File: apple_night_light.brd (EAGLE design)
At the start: 100 x 55 mm, 39 parts, among them U2 INA219AIDCNR, U3 ATSHA204-TSU, Y1 16MHZ

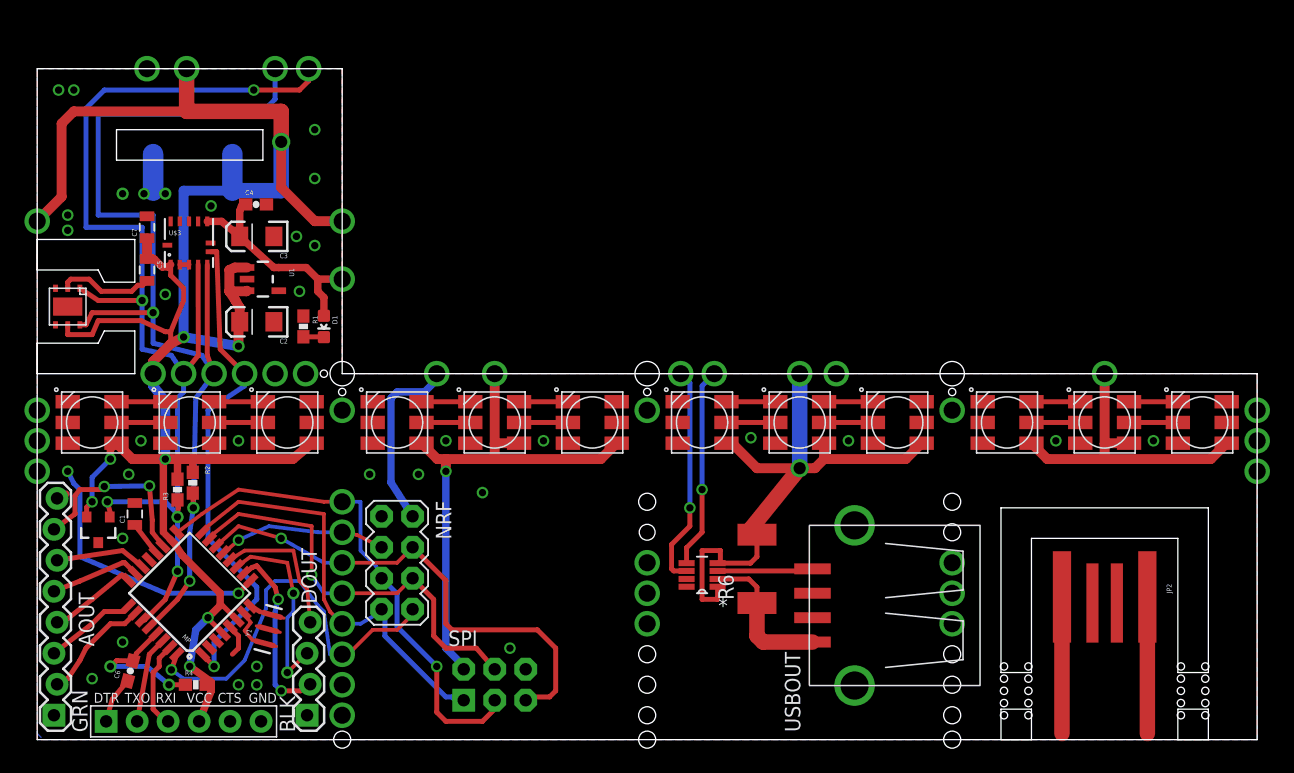
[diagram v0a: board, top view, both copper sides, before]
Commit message: re-laying out the board and separating panels to an extent
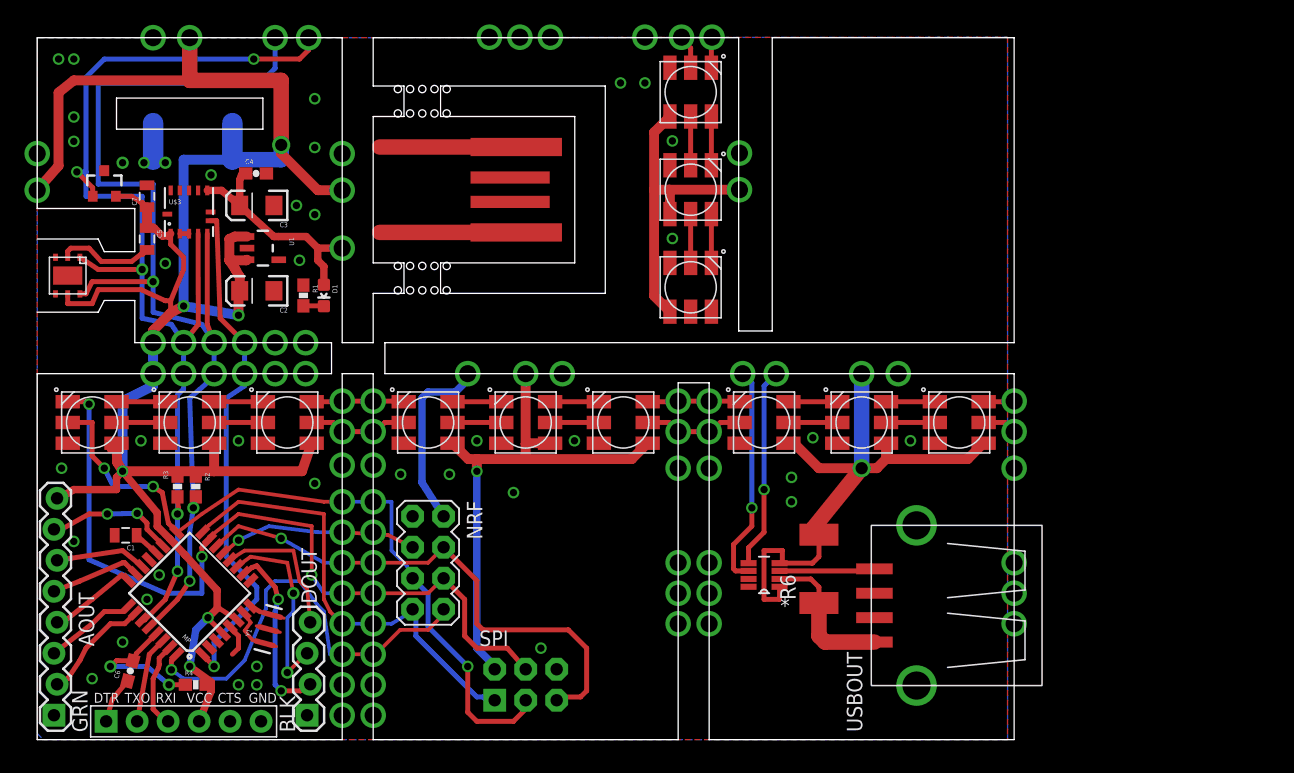
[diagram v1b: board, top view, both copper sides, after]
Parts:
- moved JP2 58.9 mm to (39.1, 45.1), turned to 180 degrees
- moved LED12 43.4 mm to (53.6, 37.1), turned to 90 degrees
- moved LED11 38.9 mm to (53.6, 45.1), turned to 90 degrees
- moved LED10 37.5 mm to (53.6, 53.1), turned to 90 degrees
- moved U3 28.3 mm to (5.50, 45.5), turned to 0 degrees
- moved LED7 5.08 mm to (59.6, 26.0)
- moved LED8 5.08 mm to (67.6, 26.0)
- moved LED9 5.08 mm to (75.6, 26.0)
- moved R6 5.08 mm to (64.1, 14.0)
- moved U2 5.08 mm to (59.6, 13.5)
- moved USBOUT 5.08 mm to (72.1, 11.0)
- moved C2 2.54 mm to (18.0, 36.8)
- moved C3 2.54 mm to (18.0, 43.8)
- moved C4 2.54 mm to (17.9, 46.4)
- moved C5 2.54 mm to (9.00, 41.0)
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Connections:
- removed net APACI: LED1.5
- removed net APADI: LED1.4
- net MOSI: now also LED1.4
- net SCK: now also LED1.5
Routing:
- net MOSI: track 34.5 -> 66.4 mm, vias 2 -> 4
- net NPIN: track 22.4 -> 0.00 mm, vias 2 -> 0
- net SCK: track 42.2 -> 60.3 mm, vias 2 -> 4
- net APACI2: track 0.00 -> 8.16 mm
- net APACI1: track 0.00 -> 8.16 mm
- net N$8: track 0.00 -> 7.58 mm
- net N$6: track 0.00 -> 7.58 mm
- net +5V: track 304.3 -> 311.1 mm, vias 17 -> 15
- net APACI3: track 0.00 -> 5.57 mm
- net N$12: track 0.00 -> 5.02 mm
- net A6: track 15.3 -> 10.7 mm
- net SCL: track 102.6 -> 105.3 mm
- net IRQ: track 32.6 -> 35.3 mm
- net MISO: track 35.0 -> 37.6 mm
- net CSN: track 41.4 -> 43.9 mm
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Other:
- board size 100 x 55 mm -> 80.1 x 57.5 mm

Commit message: adding balance board for space usage, tightening things up
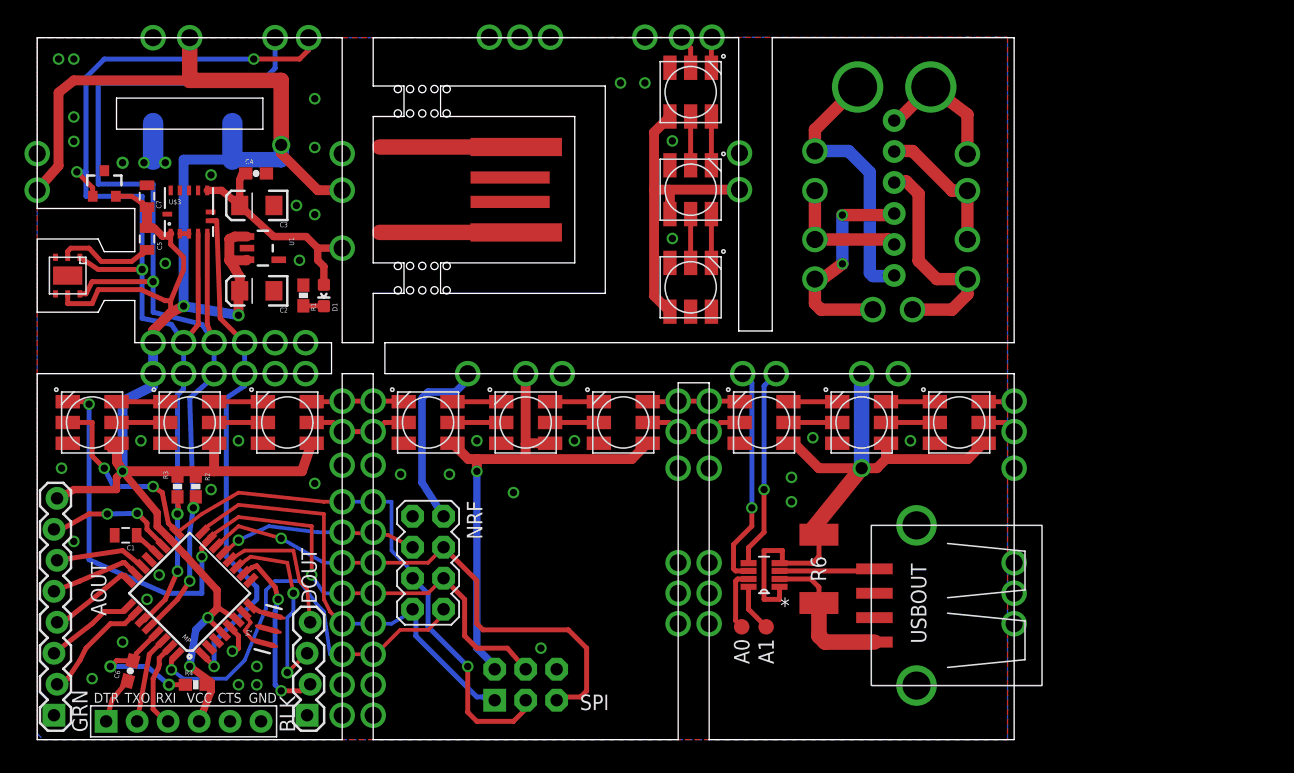
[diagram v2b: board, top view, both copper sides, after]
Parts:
- added A0, A1: TPB1,27, testpad:B1,27
- added JP3: (no value), SparkFun-Connectors:1X06_NO_SILK
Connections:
- new net N$43: A0.TP, U2.7
- new net N$44: A1.TP, U2.8
- new net N$46: AOUT.1, C1.2, C2.C, C3.C, C4.2, C5.2, C7.2, DOUT.1, JP1.P$5, JP1.P$6, JP2.GND, LED1.6, LED10.6, LED11.6, LED12.6, LED2.6, LED3.6, LED4.6, LED5.6, LED6.6, LED7.6, LED8.6, LED9.6, MP.21, MP.3, MP.5, NRF.1, R1.1, SPI.6, U$1.P$2, U$3.12, U$3.13, U$3.2, U$3.3, U1.2, U2.3, USBOUT.GND, Y1.2
- net GND: now also JP3.1; no longer AOUT.1, C1.2, C2.C, C3.C, C4.2, C5.2, C7.2, DOUT.1, JP1.P$5, JP1.P$6, JP2.GND, LED1.6, LED10.6, LED11.6, LED12.6, LED2.6, LED3.6, LED4.6, LED5.6, LED6.6, LED7.6, LED8.6, LED9.6, MP.21, MP.3, MP.5, NRF.1, R1.1, SPI.6, U$1.P$2, U$3.12, U$3.13, U$3.2, U$3.3, U1.2, U2.3, USBOUT.GND, Y1.2
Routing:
- net N$46: track 0.00 -> 40.6 mm, vias 0 -> 76
- net GND: track 33.6 -> 4.14 mm, vias 72 -> 0
- net N$55: track 0.00 -> 22.3 mm, vias 0 -> 2
- net N$49: track 0.00 -> 18.8 mm, vias 0 -> 2
- net N$51: track 0.00 -> 17.8 mm, vias 0 -> 3
- net N$47: track 0.00 -> 7.35 mm, vias 0 -> 1
- net N$45: track 0.00 -> 6.96 mm
- net N$43: track 0.00 -> 5.09 mm
- net N$48: track 0.00 -> 4.25 mm, vias 0 -> 1
- net N$53: track 0.00 -> 4.00 mm, vias 0 -> 2
- net N$44: track 0.00 -> 3.88 mm
- added copper zone on layer 1, net N$46
- added copper zone on layer 16, net N$46
- removed copper zone on layer 1, net GND
- removed copper zone on layer 16, net GND
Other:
- board text added: "+"
- board text added: "-"
- board text added: "5s balance board"
- board text added: "CUT OUT"

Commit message: final changes before order, reversing tx/rx for ftdi, reset pin on SPI
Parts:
- moved C6 0.10 mm to (7.53, 5.63), turned to 61.1 degrees
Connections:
- removed net N$22: C6.2, MP.29, R4.1
- removed net N$46: AOUT.1, C1.2, C2.C, C3.C, C4.2, C5.2, C7.2, DOUT.1, JP1.P$5, JP1.P$6, JP2.GND, LED1.6, LED10.6, LED11.6, LED12.6, LED2.6, LED3.6, LED4.6, LED5.6, LED6.6, LED7.6, LED8.6, LED9.6, MP.21, MP.3, MP.5, NRF.1, R1.1, SPI.6, U$1.P$2, U$3.12, U$3.13, U$3.2, U$3.3, U1.2, U2.3, USBOUT.GND, Y1.2
- new net RESET: C6.2, MP.29, R4.1, SPI.5
- net CSN: no longer SPI.5
- net GND: now also AOUT.1, C1.2, C2.C, C3.C, C4.2, C5.2, C7.2, DOUT.1, JP1.P$5, JP1.P$6, JP2.GND, LED1.6, LED10.6, LED11.6, LED12.6, LED2.6, LED3.6, LED4.6, LED5.6, LED6.6, LED7.6, LED8.6, LED9.6, MP.21, MP.3, MP.5, NRF.1, R1.1, SPI.6, U$1.P$2, U$3.12, U$3.13, U$3.2, U$3.3, U1.2, U2.3, USBOUT.GND, Y1.2
- net RXI: now also JP1.P$3; no longer JP1.P$2
- net TXO: now also JP1.P$2; no longer JP1.P$3
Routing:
- net RESET: track 0.00 -> 47.9 mm, vias 0 -> 4
- net N$46: track 40.6 -> 0.00 mm, vias 76 -> 0
- net GND: track 4.14 -> 44.7 mm, vias 0 -> 75
- net CSN: track 43.9 -> 20.4 mm
- net N$22: track 11.7 -> 0.00 mm, vias 2 -> 0
- net RXI: track 7.17 -> 8.15 mm, vias 0 -> 1
- added copper zone on layer 1, net GND
- added copper zone on layer 16, net GND
- removed copper zone on layer 1, net N$46
- removed copper zone on layer 16, net N$46
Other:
- outline, holes or cut-outs redrawn
- board text added: "5V"
- board text added: "A0"
- board text added: "A1"
- board text added: "A2"
- board text added: "A3"
- board text added: "A6"
- board text added: "A7"
- board text added: "D6"
- board text added: "D7"
- board text added: "D8"

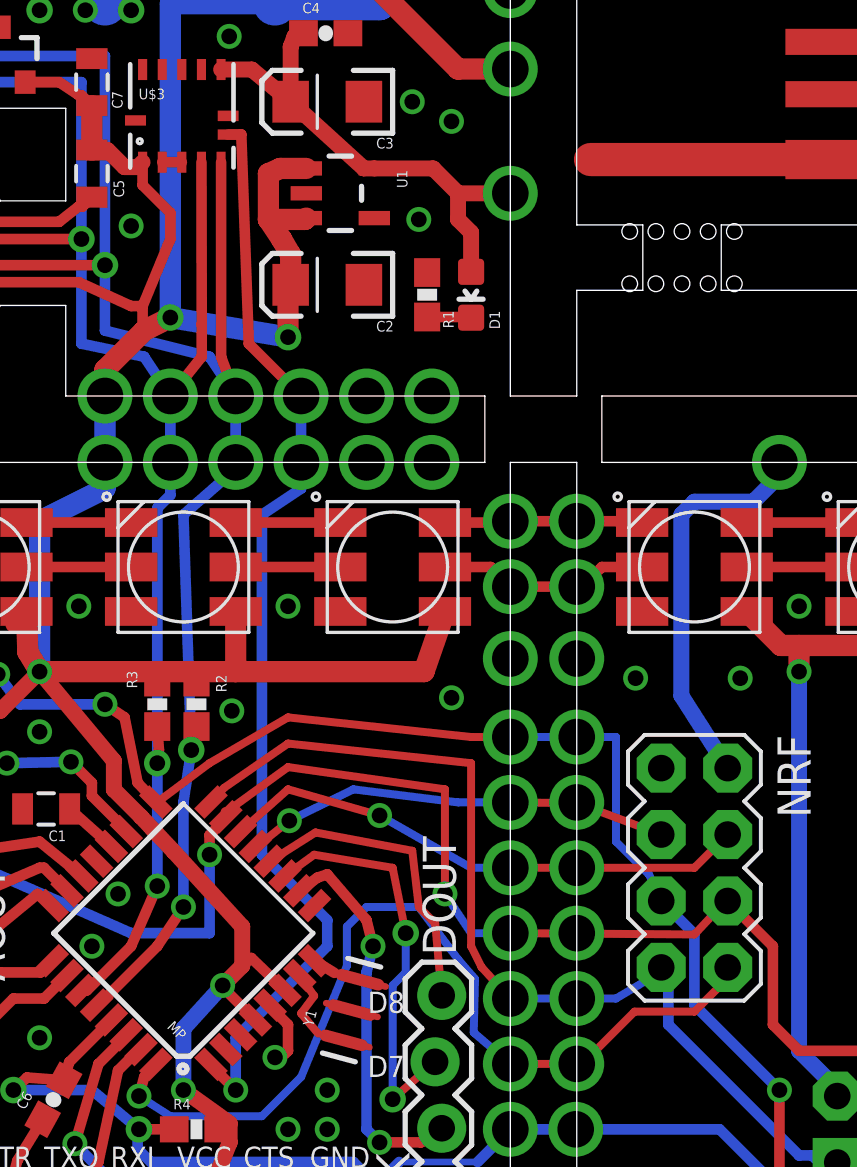
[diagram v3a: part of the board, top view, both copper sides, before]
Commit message: fixing issue with grounding VCNL IR emmiter, causes blow out of emmiter :x
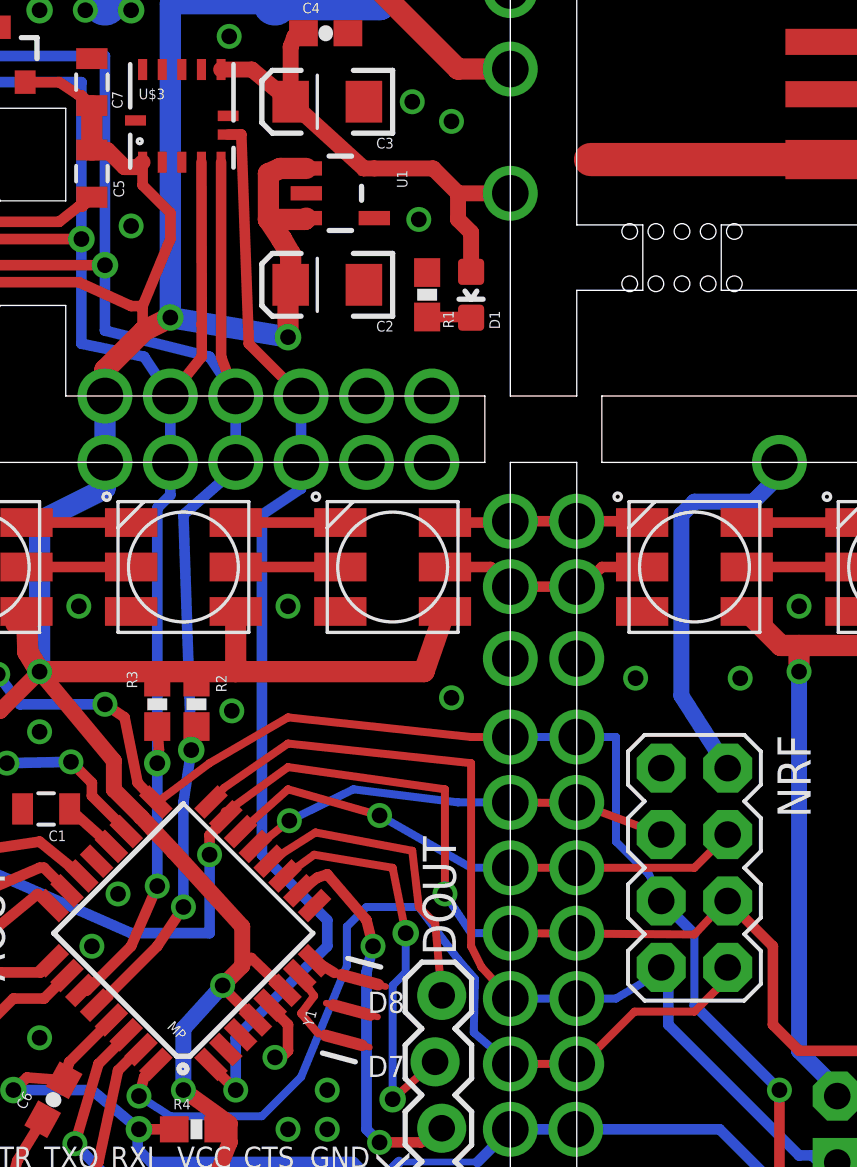
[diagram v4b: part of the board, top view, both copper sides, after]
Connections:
- new net IR-: U$3.2, U$3.3
- net GND: no longer U$3.2, U$3.3
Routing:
- net GND: track 44.7 -> 44.0 mm
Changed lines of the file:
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@@
 <via x="35.29" y="6" extent="1-16" drill="0.6"/>
 <wire x1="35.29" y1="6" x2="32.04" y2="9.25" width="0.4064" layer="16"/>
-<wire x1="32.04" y1="9.25" x2="32.04" y2="12" width="0.4064" layer="16"/>
+<wire x1="32.04" y1="9.25" x2="32.04" y2="12" width="0.3048" layer="16"/>
 <wire x1="32.04" y1="12" x2="32" y2="12" width="0.4064" layer="16"/>
 <wire x1="32" y1="12" x2="30.77" y2="13.23" width="0.4064" layer="16"/>
@@
 <contactref element="NRF" pad="1"/>
 <via x="25" y="2" extent="1-16" drill="1.4"/>
-<contactref element="U$3" pad="3"/>
-<contactref element="U$3" pad="2"/>
-<wire x1="11.69" y1="41.4775" x2="12.44" y2="41.4775" width="0.4064" layer="1"/>
 <wire x1="39.265" y1="41.58" x2="28.065" y2="41.58" width="1.27" layer="1"/>
 <via x="19.5" y="32.54" extent="1-16" drill="1.4" diameter="1.4224"/>
@@
 <via x="33.79" y="21.75" extent="1-16" drill="0.6"/>
 <via x="29.79" y="21.75" extent="1-16" drill="0.6"/>
-<via x="39.04" y="20.25" extent="1-16" drill="0.6"/>
+<via x="39.04" y="20.25" extent="1-16" drill="0.6" alwaysstop="yes"/>
 <via x="1.75" y="55.79" extent="1-16" drill="0.6"/>
 <via x="3" y="51.04" extent="1-16" drill="0.6"/>
@@
 <wire x1="69.75" y1="41" x2="70.25" y2="40.5" width="1.016" layer="1"/>
 </signal>
+<signal name="IR-">
+<contactref element="U$3" pad="2"/>
+<contactref element="U$3" pad="3"/>
+<wire x1="12.44" y1="41.4775" x2="11.69" y2="41.4775" width="0" layer="19" extent="1-1"/>
+</signal>
 </signals>
